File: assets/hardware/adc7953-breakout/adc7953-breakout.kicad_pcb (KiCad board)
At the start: 2 copper layers, 45.7 x 53.3 mm, 7 parts, among them J1 Conn_01x19_Male, J2 Conn_01x19_Male, U1 ADS7953SBDBTR

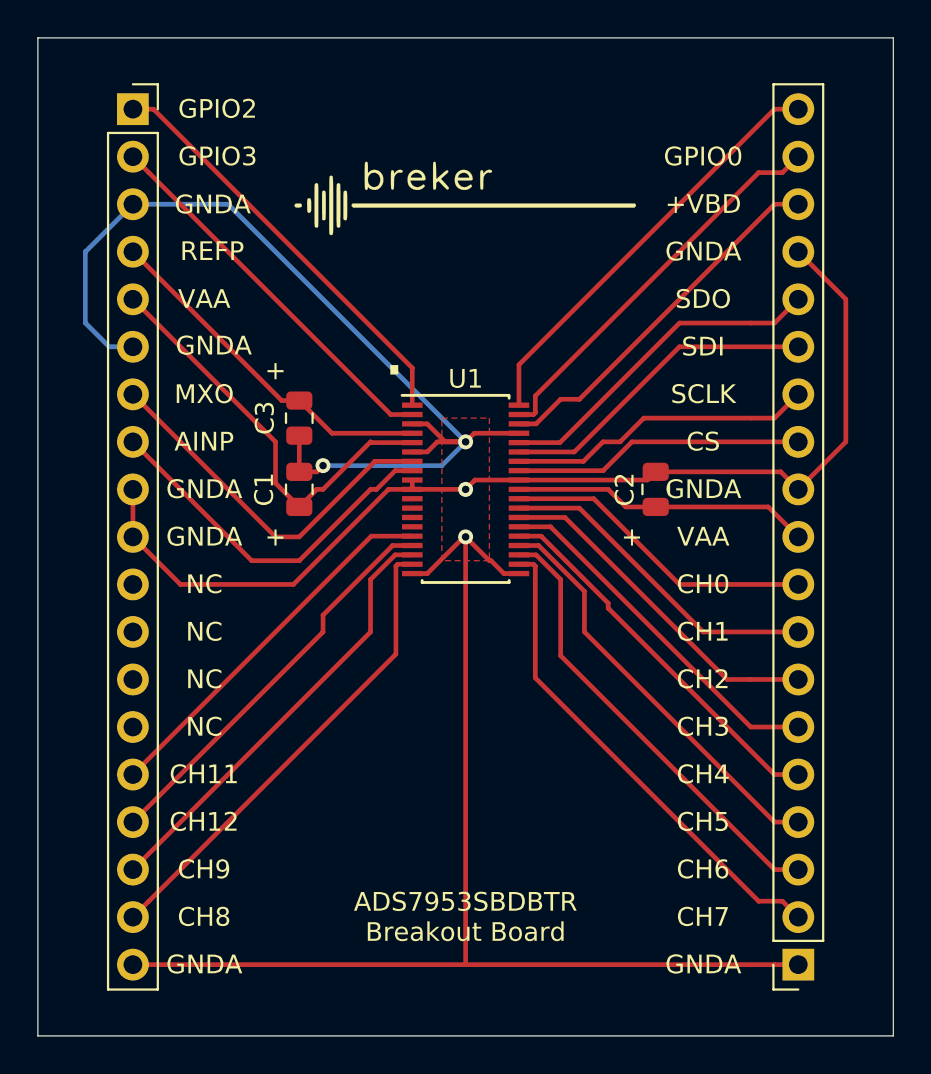
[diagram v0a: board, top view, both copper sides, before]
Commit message: moved hardware to assets and cleaned up design
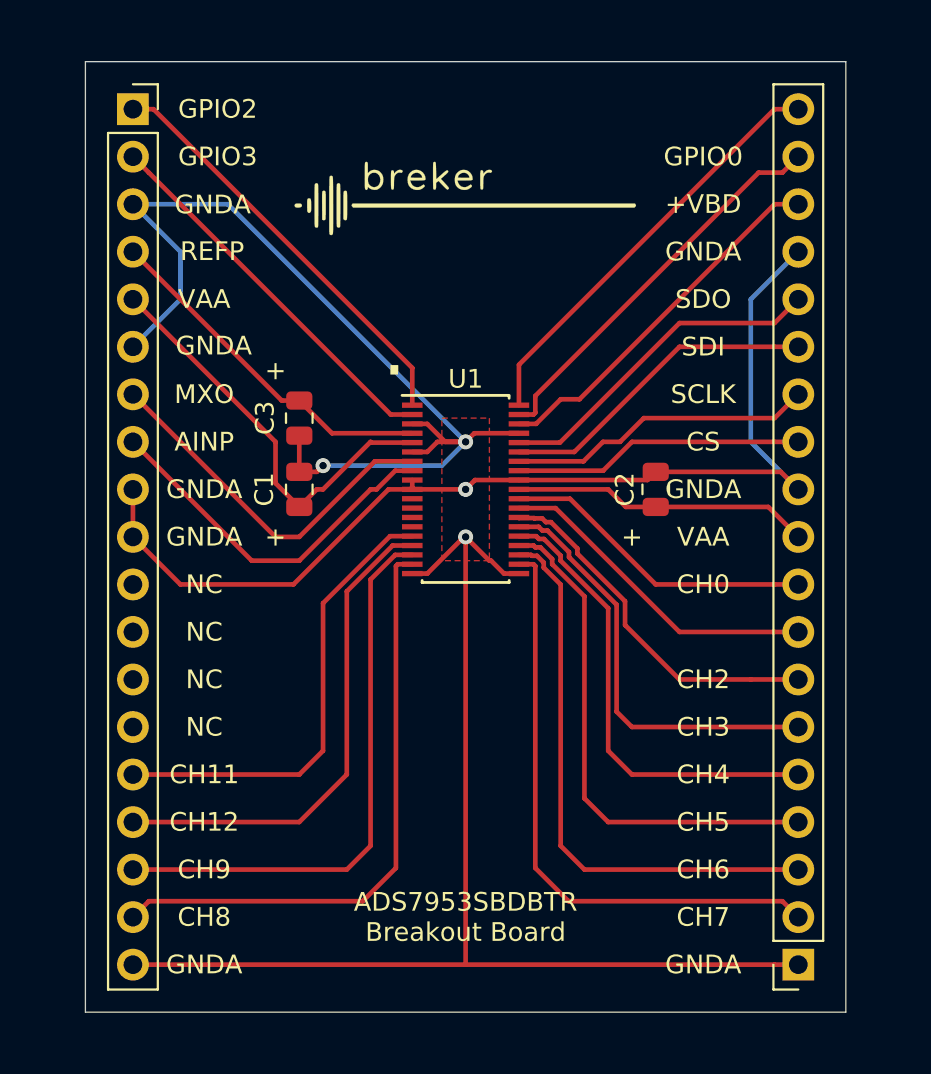
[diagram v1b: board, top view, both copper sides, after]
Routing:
- net CH8: track 25.5 -> 32.2 mm
- net CH9: track 23.5 -> 30.2 mm
- net CH7: track 26.2 -> 32.2 mm
- net CH6: track 24.3 -> 30.2 mm
- net CH5: track 22.3 -> 27.5 mm
- net CH10: track 21.6 -> 26.8 mm
- net CH11: track 20.2 -> 24.8 mm
- net CH4: track 20.4 -> 24.8 mm
- net CH3: track 19.4 -> 22.9 mm
- net CH2: track 18.5 -> 19.4 mm
- net GNDA: track 177.4 -> 176.6 mm
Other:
- board size 45.7 x 53.3 mm -> 40.6 x 50.8 mm
- board text removed: "CH1"
